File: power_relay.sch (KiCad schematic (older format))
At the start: 35 parts, among them J21 Conn_01x03, J22 Conn_01x03, J23 Conn_01x03, J24 Conn_01x03, J25 Conn_01x03, K1 RELAY_1RT, K2 RELAY_1RT, K3 RELAY_1RT, K4 RELAY_1RT, K5 RELAY_1RT, Q12 MMBT4401-7-F, Q13 MMBT4401-7-F, Q14 MMBT4401-7-F, Q15 SI7113ADN-T1-GE3, Q16 SI7113ADN-T1-GE3, Q17 SI7113ADN-T1-GE3, Q18 MMBT4401-7-F, Q19 MMBT4401-7-F, Q20 SI7113ADN-T1-GE3, Q21 SI7113ADN-T1-GE3

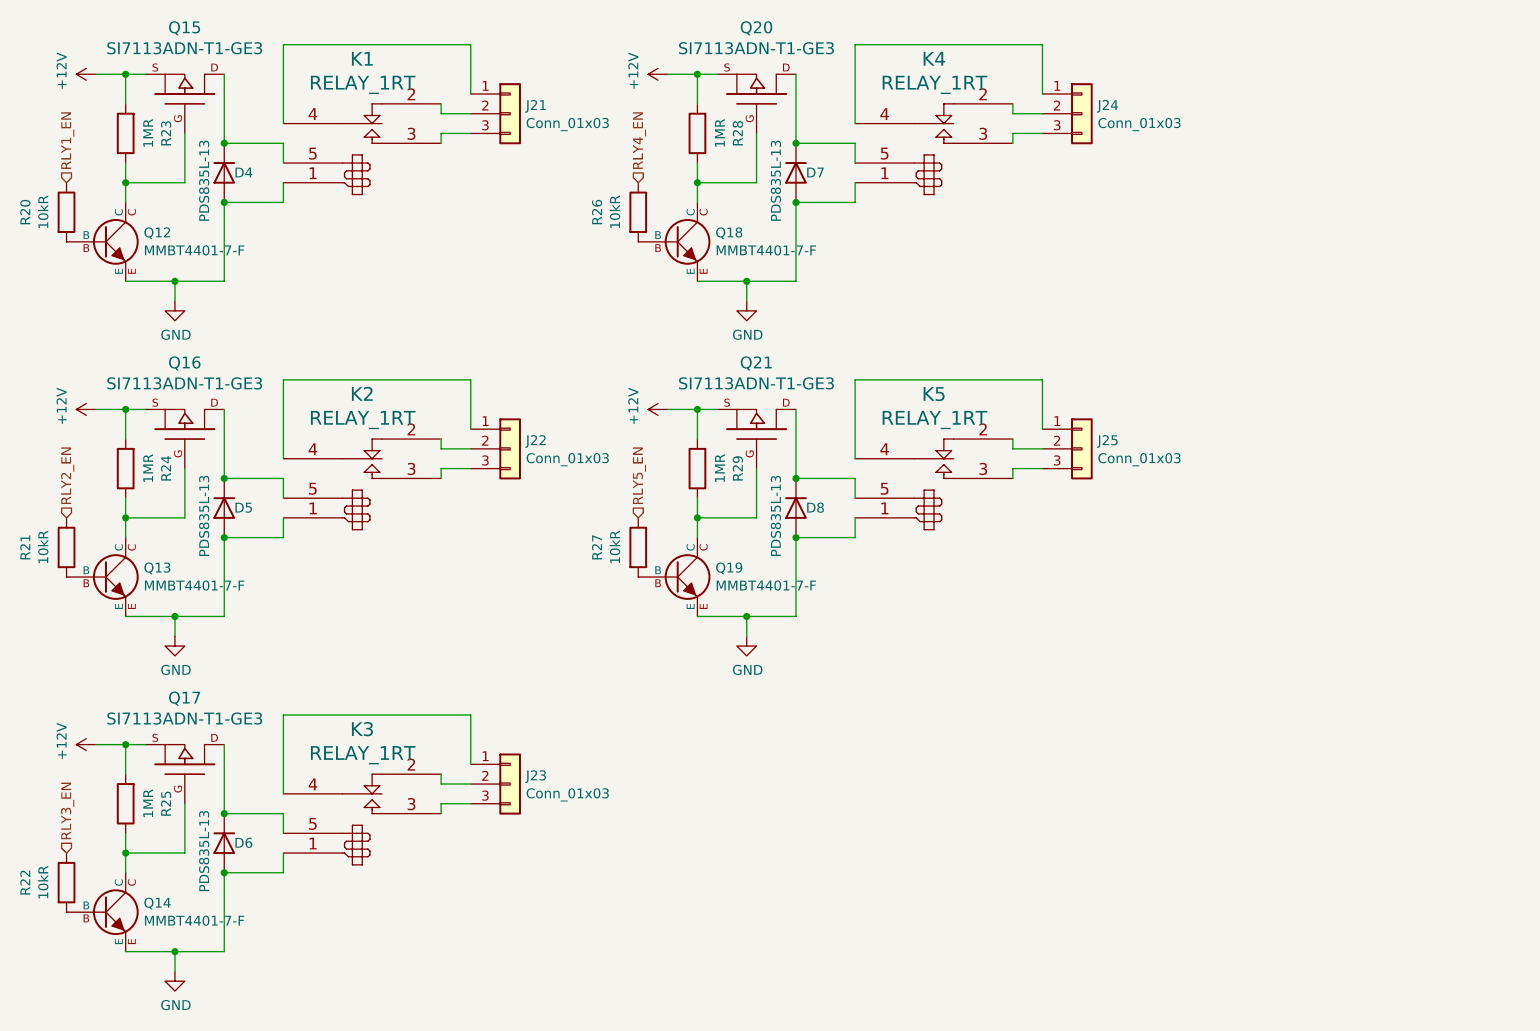
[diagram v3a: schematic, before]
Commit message: Added remaining 0603 references
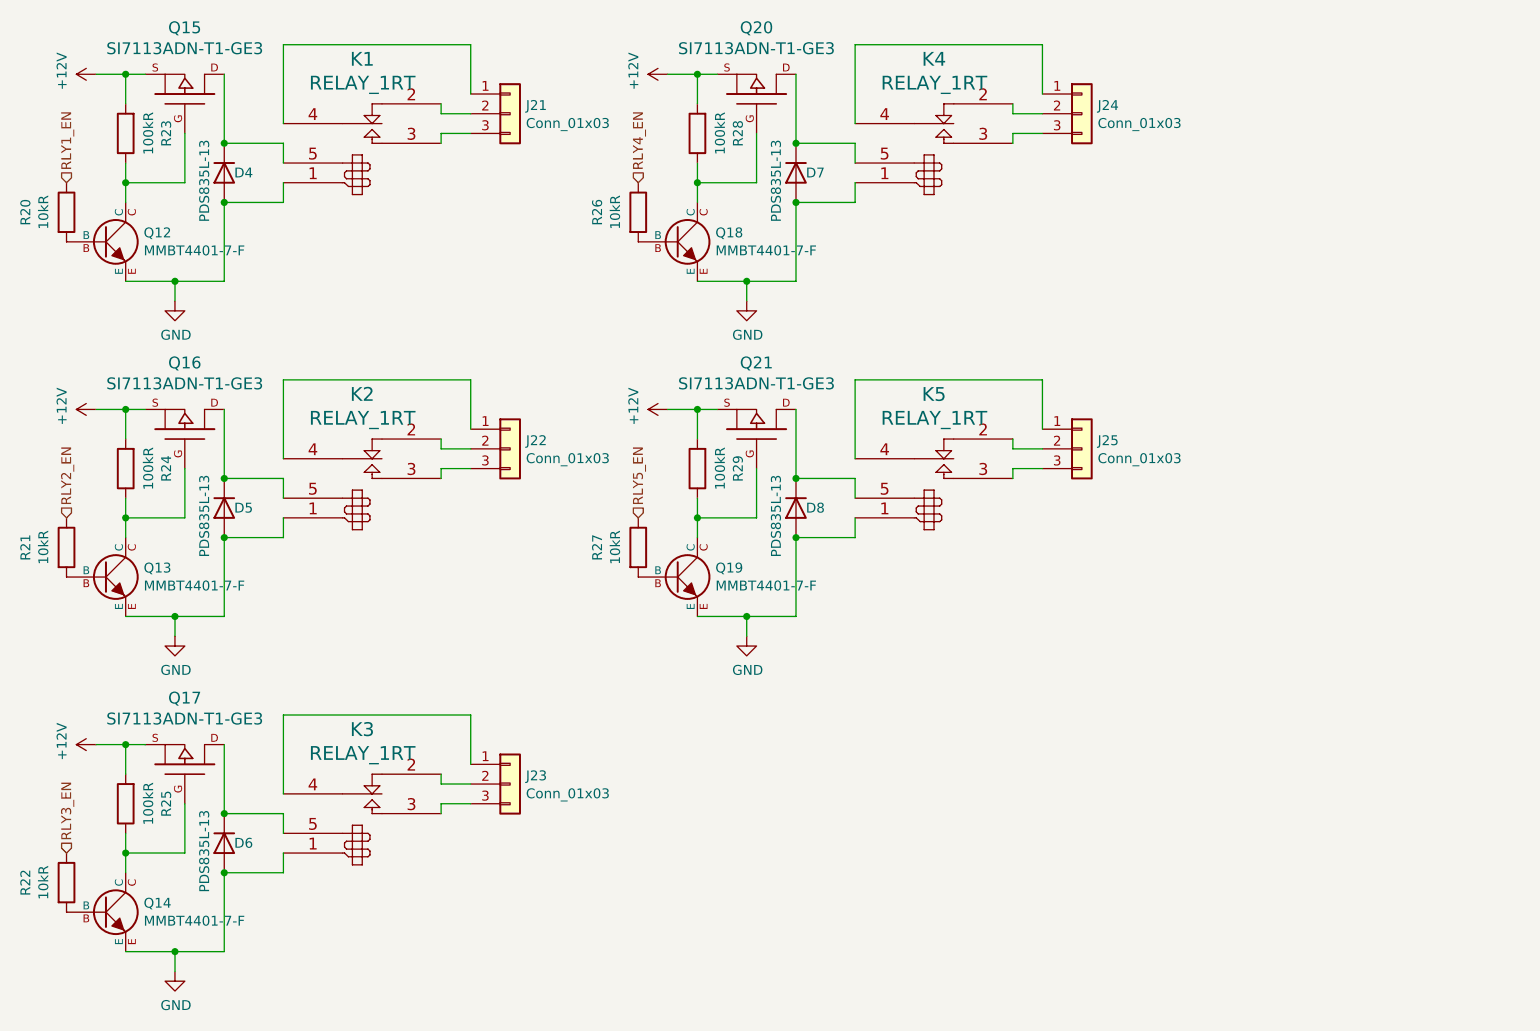
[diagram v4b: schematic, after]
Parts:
- R20, R21, R22, R26, R27: manf# (none) -> CRCW060310K0JNEBC
- R23, R24, R25, R28, R29: value 1MR -> 100kR; manf# (none) -> CRCW0603100KFKEAC
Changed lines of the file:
@@
 F 2 "lsts-passives:R_0603" V 3830 3400 50  0001 C CNN
 F 3 "~" H 3900 3400 50  0001 C CNN
+F 4 "CRCW060310K0JNEBC" H 3900 3400 50  0001 C CNN "manf#"
 	1    3900 3400
 	1    0    0    -1
@@
 AR Path="/5E4850C0/5E48FA6A" Ref="R29"  Part="1"
 F 0 "R29" V 3993 3000 50  0000 C CNN
-F 1 "1MR" V 4084 3000 50  0000 C CNN
+F 1 "100kR" V 4084 3000 50  0000 C CNN
 F 2 "lsts-passives:R_0603" V 4130 3000 50  0001 C CNN
 F 3 "~" H 4200 3000 50  0001 C CNN
+F 4 "CRCW0603100KFKEAC" H 4200 3000 50  0001 C CNN "manf#"
 	1    4200 3000
 	-1   0    0    1
@@
 F 2 "lsts-passives:R_0603" V 3830 1700 50  0001 C CNN
 F 3 "~" H 3900 1700 50  0001 C CNN
+F 4 "CRCW060310K0JNEBC" H 3900 1700 50  0001 C CNN "manf#"
 	1    3900 1700
 	1    0    0    -1
@@
 AR Path="/5E4850C0/5E48FAC2" Ref="R28"  Part="1"
 F 0 "R28" V 3993 1300 50  0000 C CNN
-F 1 "1MR" V 4084 1300 50  0000 C CNN
+F 1 "100kR" V 4084 1300 50  0000 C CNN
 F 2 "lsts-passives:R_0603" V 4130 1300 50  0001 C CNN
 F 3 "~" H 4200 1300 50  0001 C CNN
+F 4 "CRCW0603100KFKEAC" H 4200 1300 50  0001 C CNN "manf#"
 	1    4200 1300
 	-1   0    0    1
@@
 F 2 "lsts-passives:R_0603" V 930 3400 50  0001 C CNN
 F 3 "~" H 1000 3400 50  0001 C CNN
+F 4 "CRCW060310K0JNEBC" H 1000 3400 50  0001 C CNN "manf#"
 	1    1000 3400
 	1    0    0    -1
@@
 AR Path="/5E4850C0/5E48FB13" Ref="R24"  Part="1"
 F 0 "R24" V 1093 3000 50  0000 C CNN
-F 1 "1MR" V 1184 3000 50  0000 C CNN
+F 1 "100kR" V 1184 3000 50  0000 C CNN
 F 2 "lsts-passives:R_0603" V 1230 3000 50  0001 C CNN
 F 3 "~" H 1300 3000 50  0001 C CNN
+F 4 "CRCW0603100KFKEAC" H 1300 3000 50  0001 C CNN "manf#"
 	1    1300 3000
 	-1   0    0    1
@@
 F 2 "lsts-passives:R_0603" V 930 1700 50  0001 C CNN
 F 3 "~" H 1000 1700 50  0001 C CNN
+F 4 "CRCW060310K0JNEBC" H 1000 1700 50  0001 C CNN "manf#"
 	1    1000 1700
 	1    0    0    -1
@@
 AR Path="/5E4850C0/5E48FB6B" Ref="R23"  Part="1"
 F 0 "R23" V 1093 1300 50  0000 C CNN
-F 1 "1MR" V 1184 1300 50  0000 C CNN
+F 1 "100kR" V 1184 1300 50  0000 C CNN
 F 2 "lsts-passives:R_0603" V 1230 1300 50  0001 C CNN
 F 3 "~" H 1300 1300 50  0001 C CNN
+F 4 "CRCW0603100KFKEAC" H 1300 1300 50  0001 C CNN "manf#"
 	1    1300 1300
 	-1   0    0    1
@@
 F 2 "lsts-passives:R_0603" V 930 5100 50  0001 C CNN
 F 3 "~" H 1000 5100 50  0001 C CNN
+F 4 "CRCW060310K0JNEBC" H 1000 5100 50  0001 C CNN "manf#"
 	1    1000 5100
 	1    0    0    -1
@@
 AR Path="/5E4850C0/5E48FBC3" Ref="R25"  Part="1"
 F 0 "R25" V 1093 4700 50  0000 C CNN
-F 1 "1MR" V 1184 4700 50  0000 C CNN
+F 1 "100kR" V 1184 4700 50  0000 C CNN
 F 2 "lsts-passives:R_0603" V 1230 4700 50  0001 C CNN
 F 3 "~" H 1300 4700 50  0001 C CNN
+F 4 "CRCW0603100KFKEAC" H 1300 4700 50  0001 C CNN "manf#"
 	1    1300 4700
 	-1   0    0    1

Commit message: Changed "out of stock" references.
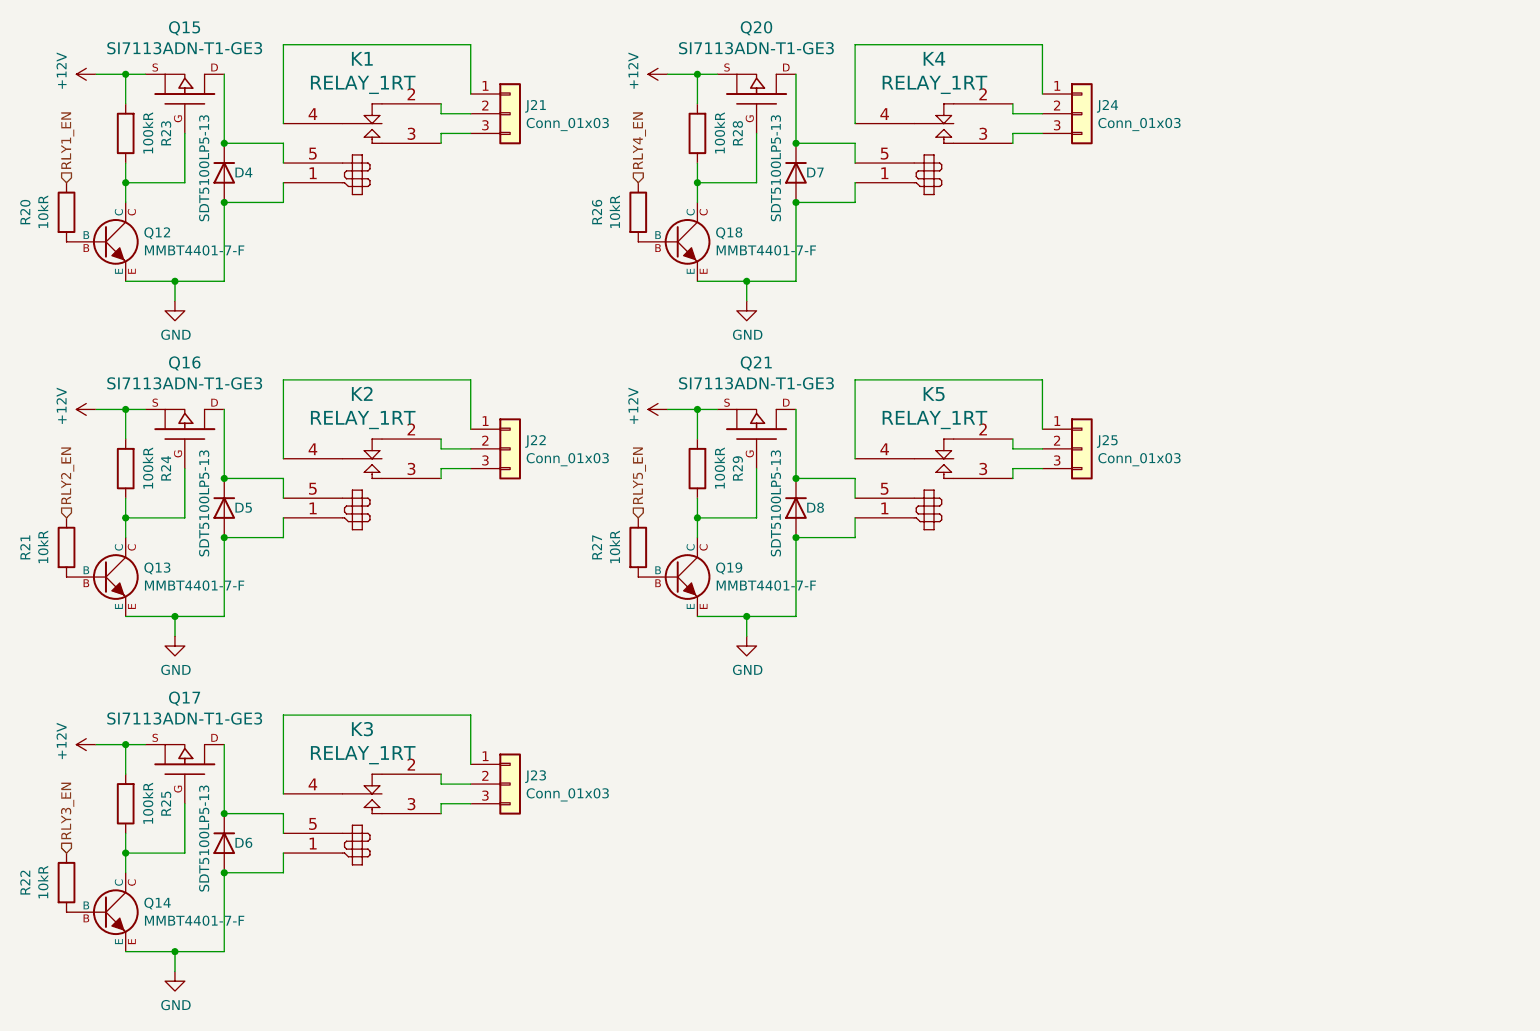
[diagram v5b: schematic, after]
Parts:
- D4, D5, D6, D7, D8: value PDS835L-13 -> SDT5100LP5-13; manf# PDS835L-13 -> SDT5100LP5-13
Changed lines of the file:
@@
 AR Path="/5E4850C0/5E48FA30" Ref="D8"  Part="1"
 F 0 "D8" V 4700 3150 50  0000 R CNN
-F 1 "PDS835L-13" H 4950 3300 50  0000 R CNN
+F 1 "SDT5100LP5-13" H 4950 3300 50  0000 R CNN
 F 2 "Diode_SMD:D_PowerDI-5" H 4700 3200 50  0001 L CNN
 F 3 "~" H 4700 3200 50  0001 C CNN
-F 4 "PDS835L-13" H 4700 3200 50  0001 C CNN "manf#"
+F 4 "SDT5100LP5-13" H 4700 3200 50  0001 C CNN "manf#"
 	1    4700 3200
 	0    -1   1    0
@@
 AR Path="/5E4850C0/5E48FA88" Ref="D7"  Part="1"
 F 0 "D7" V 4700 1450 50  0000 R CNN
-F 1 "PDS835L-13" H 4950 1600 50  0000 R CNN
+F 1 "SDT5100LP5-13" H 4950 1600 50  0000 R CNN
 F 2 "Diode_SMD:D_PowerDI-5" H 4700 1500 50  0001 L CNN
 F 3 "~" H 4700 1500 50  0001 C CNN
-F 4 "PDS835L-13" H 4700 1500 50  0001 C CNN "manf#"
+F 4 "SDT5100LP5-13" H 4700 1500 50  0001 C CNN "manf#"
 	1    4700 1500
 	0    -1   1    0
@@
 AR Path="/5E4850C0/5E48FAE0" Ref="D5"  Part="1"
 F 0 "D5" V 1800 3150 50  0000 R CNN
-F 1 "PDS835L-13" H 2050 3300 50  0000 R CNN
+F 1 "SDT5100LP5-13" H 2050 3300 50  0000 R CNN
 F 2 "Diode_SMD:D_PowerDI-5" H 1800 3200 50  0001 L CNN
 F 3 "~" H 1800 3200 50  0001 C CNN
-F 4 "PDS835L-13" H 1800 3200 50  0001 C CNN "manf#"
+F 4 "SDT5100LP5-13" H 1800 3200 50  0001 C CNN "manf#"
 	1    1800 3200
 	0    -1   1    0
@@
 AR Path="/5E4850C0/5E48FB31" Ref="D4"  Part="1"
 F 0 "D4" V 1800 1450 50  0000 R CNN
-F 1 "PDS835L-13" H 2050 1600 50  0000 R CNN
+F 1 "SDT5100LP5-13" H 2050 1600 50  0000 R CNN
 F 2 "Diode_SMD:D_PowerDI-5" H 1800 1500 50  0001 L CNN
 F 3 "~" H 1800 1500 50  0001 C CNN
-F 4 "PDS835L-13" H 1800 1500 50  0001 C CNN "manf#"
+F 4 "SDT5100LP5-13" H 1800 1500 50  0001 C CNN "manf#"
 	1    1800 1500
 	0    -1   1    0
@@
 AR Path="/5E4850C0/5E48FB89" Ref="D6"  Part="1"
 F 0 "D6" V 1800 4850 50  0000 R CNN
-F 1 "PDS835L-13" H 2050 5000 50  0000 R CNN
+F 1 "SDT5100LP5-13" H 2050 5000 50  0000 R CNN
 F 2 "Diode_SMD:D_PowerDI-5" H 1800 4900 50  0001 L CNN
 F 3 "~" H 1800 4900 50  0001 C CNN
-F 4 "PDS835L-13" H 1800 4900 50  0001 C CNN "manf#"
+F 4 "SDT5100LP5-13" H 1800 4900 50  0001 C CNN "manf#"
 	1    1800 4900
 	0    -1   1    0

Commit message: Small changes and added labels
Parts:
- K1, K2, K3, K4, K5: value RELAY_1RT -> lsts-devices:RELAY_1RT
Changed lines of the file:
@@
 AR Path="/5E4850C0/5E48FA40" Ref="K5"  Part="1"
 F 0 "K5" H 5400 3176 70  0000 C CNN
-F 1 "RELAY_1RT" H 5400 3055 70  0000 C CNN
+F 1 "lsts-devices:RELAY_1RT" H 5400 3055 70  0000 C CNN
 F 2 "Relay_THT:Relay_SPDT_Panasonic_JW1_FormC_lsts" H 5400 2900 60  0001 C CNN
 F 3 "https://pt.mouser.com/datasheet/2/315/panasonic%20electric%20works_jw-catalog-1196972.pdf" H 5400 2900 60  0001 C CNN
@@
 AR Path="/5E4850C0/5E48FA98" Ref="K4"  Part="1"
 F 0 "K4" H 5400 1476 70  0000 C CNN
-F 1 "RELAY_1RT" H 5400 1355 70  0000 C CNN
+F 1 "lsts-devices:RELAY_1RT" H 5400 1355 70  0000 C CNN
 F 2 "Relay_THT:Relay_SPDT_Panasonic_JW1_FormC_lsts" H 5400 1200 60  0001 C CNN
 F 3 "https://pt.mouser.com/datasheet/2/315/panasonic%20electric%20works_jw-catalog-1196972.pdf" H 5400 1200 60  0001 C CNN
@@
 AR Path="/5E4850C0/5E48FAF0" Ref="K2"  Part="1"
 F 0 "K2" H 2500 3176 70  0000 C CNN
-F 1 "RELAY_1RT" H 2500 3055 70  0000 C CNN
+F 1 "lsts-devices:RELAY_1RT" H 2500 3055 70  0000 C CNN
 F 2 "Relay_THT:Relay_SPDT_Panasonic_JW1_FormC_lsts" H 2500 2900 60  0001 C CNN
 F 3 "https://pt.mouser.com/datasheet/2/315/panasonic%20electric%20works_jw-catalog-1196972.pdf" H 2500 2900 60  0001 C CNN
@@
 AR Path="/5E4850C0/5E48FB41" Ref="K1"  Part="1"
 F 0 "K1" H 2500 1476 70  0000 C CNN
-F 1 "RELAY_1RT" H 2500 1355 70  0000 C CNN
+F 1 "lsts-devices:RELAY_1RT" H 2500 1355 70  0000 C CNN
 F 2 "Relay_THT:Relay_SPDT_Panasonic_JW1_FormC_lsts" H 2500 1200 60  0001 C CNN
 F 3 "https://pt.mouser.com/datasheet/2/315/panasonic%20electric%20works_jw-catalog-1196972.pdf" H 2500 1200 60  0001 C CNN
@@
 AR Path="/5E4850C0/5E48FB99" Ref="K3"  Part="1"
 F 0 "K3" H 2500 4876 70  0000 C CNN
-F 1 "RELAY_1RT" H 2500 4755 70  0000 C CNN
+F 1 "lsts-devices:RELAY_1RT" H 2500 4755 70  0000 C CNN
 F 2 "Relay_THT:Relay_SPDT_Panasonic_JW1_FormC_lsts" H 2500 4600 60  0001 C CNN
 F 3 "https://pt.mouser.com/datasheet/2/315/panasonic%20electric%20works_jw-catalog-1196972.pdf" H 2500 4600 60  0001 C CNN

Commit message: Final touches
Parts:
- removed D6, D7, D8: SDT5100LP5-13, Diode_SMD:D_PowerDI-5, symbol Device:D
- removed J25: Conn_01x03, TerminalBlock_Phoenix:TerminalBlock_Phoenix_PT-1,5-3-3.5-H_1x03_P3.50mm_Horizontal, symbol Connector_Generic:Conn_01x03
- removed K1, K2, K3, K4, K5: lsts-devices:RELAY_1RT, Relay_THT:Relay_SPDT_Panasonic_JW1_FormC_lsts, symbol lsts-devices:RELAY_1RT
- removed Q12, Q13, Q14, Q18, Q19: MMBT4401-7-F, lsts-discretes:SOT23_BC817, symbol lsts-discrete:NPN_EBC
- removed Q15, Q16, Q17, Q20, Q21: SI7113ADN-T1-GE3, lsts-discretes:PowerPAK_1212-8, symbol lsts-discrete:MOS_P
- added D1, D2, D3: SDT5100LP5-13, Diode_SMD:D_PowerDI-5, symbol Device:D
- added J20: Conn_01x03, TerminalBlock_Phoenix:TerminalBlock_Phoenix_PT-1,5-3-3.5-H_1x03_P3.50mm_Horizontal, symbol Connector_Generic:Conn_01x03
- added K1, K2, K3, K4, K5: SANYOU_SRD_Form_C, Relay_THT:Relay_SPDT_SANYOU_SRD_Series_Form_C, symbol Relay:SANYOU_SRD_Form_C
- added Q12, Q13, Q14, Q15, Q16: Q_NMOS_GDS, Package_TO_SOT_SMD:TO-252-2, symbol Device:Q_NMOS_GDS
- R20, R21: value 10kR -> 600R; footprint lsts-passives:R_0603 -> lsts_passives:R_0603; manf# CRCW060310K0JNEBC -> CRCW0603100KFKEAC
- R22, R26, R27: value 10kR -> 60kR; footprint lsts-passives:R_0603 -> lsts_passives:R_0603; manf# CRCW060310K0JNEBC -> CRCW0603100KFKEAC
- R23, R29: value 100kR -> 60kR; footprint lsts-passives:R_0603 -> lsts_passives:R_0603
- R24, R25, R28: value 100kR -> 600R; footprint lsts-passives:R_0603 -> lsts_passives:R_0603
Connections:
- net GND: now also R22.1, R23.1, R26.1, R27.1, R29.1, Q12.3 (S), Q13.3 (S), Q14.3 (S), Q15.3 (S), Q16.3 (S); no longer D4.2 (A), D5.2 (A)
- net RLY3_EN: now also R24.1; no longer R22.1
- net RLY4_EN: now also R25.1; no longer R26.1
- net RLY5_EN: now also R28.1; no longer R27.1
- net at R27.2: now also R25.2, Q15.1 (G)
- net at J24.2 (Pin_2): now also K5.1
- net at J24.3 (Pin_3): now also K5.4
- net at J24.1 (Pin_1): now also K5.3
- net at R26.2: now also R24.2, Q14.1 (G)
- net +5V: now reaches D5.1 (K)
- net +5V: now also D4.1 (K), D1.1 (K), D2.1 (K), D3.1 (K), K1.5, K2.5, K3.5, K4.5, K5.5
- net at J22.2 (Pin_2): now also K3.1
- net at J22.3 (Pin_3): now also K3.4
- net at J22.1 (Pin_1): now also K3.3
- net at R21.2: now also R23.2, Q13.1 (G)
- net at J21.2 (Pin_2): now also K2.1
- net at J21.3 (Pin_3): now also K2.4
- net at J21.1 (Pin_1): now also K2.3
- net at R20.2: now also R22.2, Q12.1 (G)
- net at J23.2 (Pin_2): now also K4.1
- net at J23.3 (Pin_3): now also K4.4
- net at J23.1 (Pin_1): now also K4.3
- removed net +12V: R23.2, R24.2, R25.2, R28.2, R29.2
- new net: J20.2 (Pin_2), K1.1
- new net: D1.2 (A), K1.2, Q12.2 (D)
- new net: J20.1 (Pin_1), K1.3
- new net: J20.3 (Pin_3), K1.4
- new net: D3.2 (A), K3.2, Q14.2 (D)
- new net: D5.2 (A), K5.2, Q16.2 (D)
- new net: Q16.1 (G), R28.2, R29.2
- new net: D2.2 (A), K2.2, Q13.2 (D)
- new net: D4.2 (A), K4.2, Q15.2 (D)
